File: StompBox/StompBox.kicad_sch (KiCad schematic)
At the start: 43 parts, among them J1 AudioJack2_Dual_Ground_Switch, J2 Barrel_Jack_Switch, J3 Conn_01x03, J4 AudioJack2_Dual_Ground_Switch, J5 BATT, SW1 ThreeWayStompBox, SW2 ThreeWayStompBox, SW3 ThreeWayStompBox, SW4 ThreeWayStompBox

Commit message: Stompbox JLCPCB
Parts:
- added H10, H11, H12, H9: MountingHole, MountingHole:MountingHole_3.2mm_M3, symbol Mechanical:MountingHole
- added J6: AudioJack2_Dual_Ground_Switch, StompBox:PJ-3240-35mm-stereo, symbol Connector:AudioJack2_Dual_Ground_Switch
- added R14: 10k, Resistor_THT:R_Axial_DIN0207_L6.3mm_D2.5mm_P7.62mm_Horizontal, symbol Device:R
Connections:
- net OUTVOLT is gone; now on net INVOLT: C1.1, J1.T1, J3.2 (Pin_2), JP2.1 (A)
- net GND: now also J6.G
- net at C3.1, J4.T1, R8.2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: now also R7.1, R14.1
- net at JP1.2 (B), R8.1: no longer R7.1
- new net: J6.T1, R14.2
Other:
- moved on the sheet: H1, H2, H3, H4, H5, H6, H7, H8

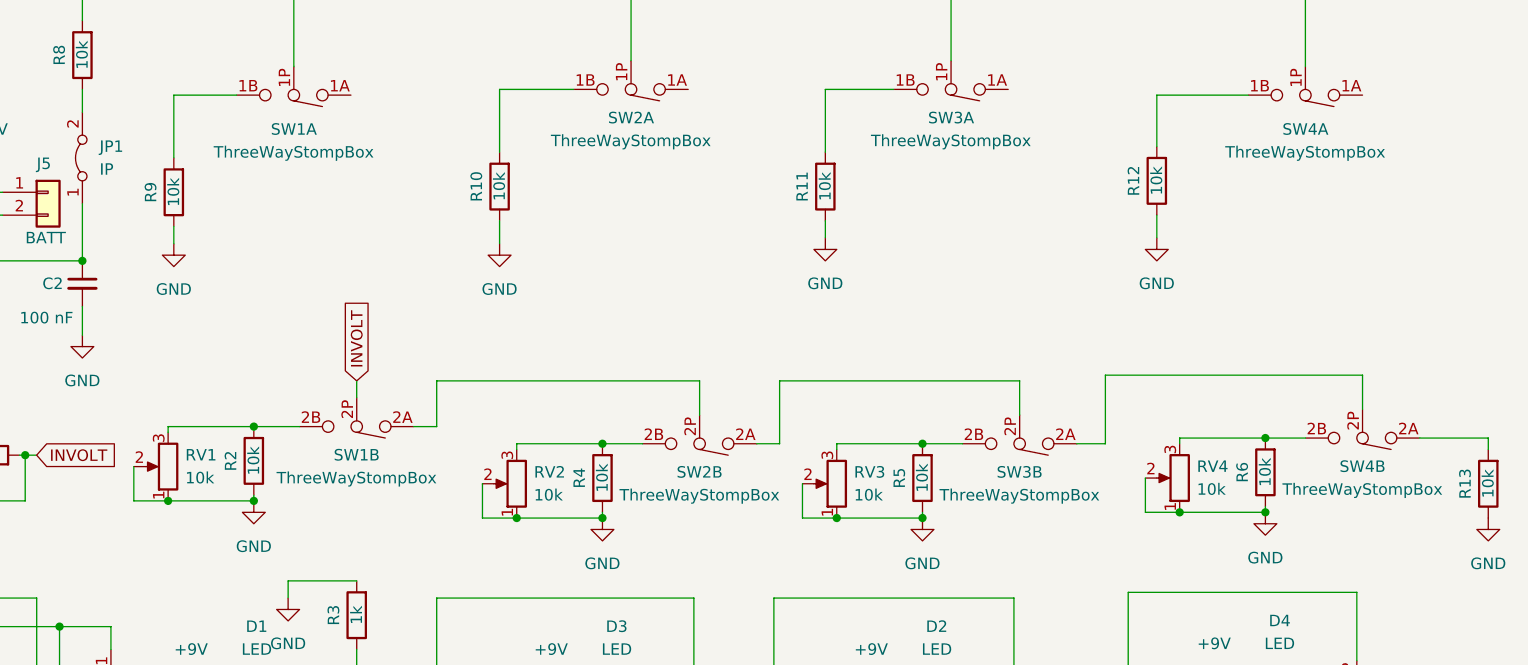
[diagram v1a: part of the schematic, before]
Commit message: Added support for stomp box
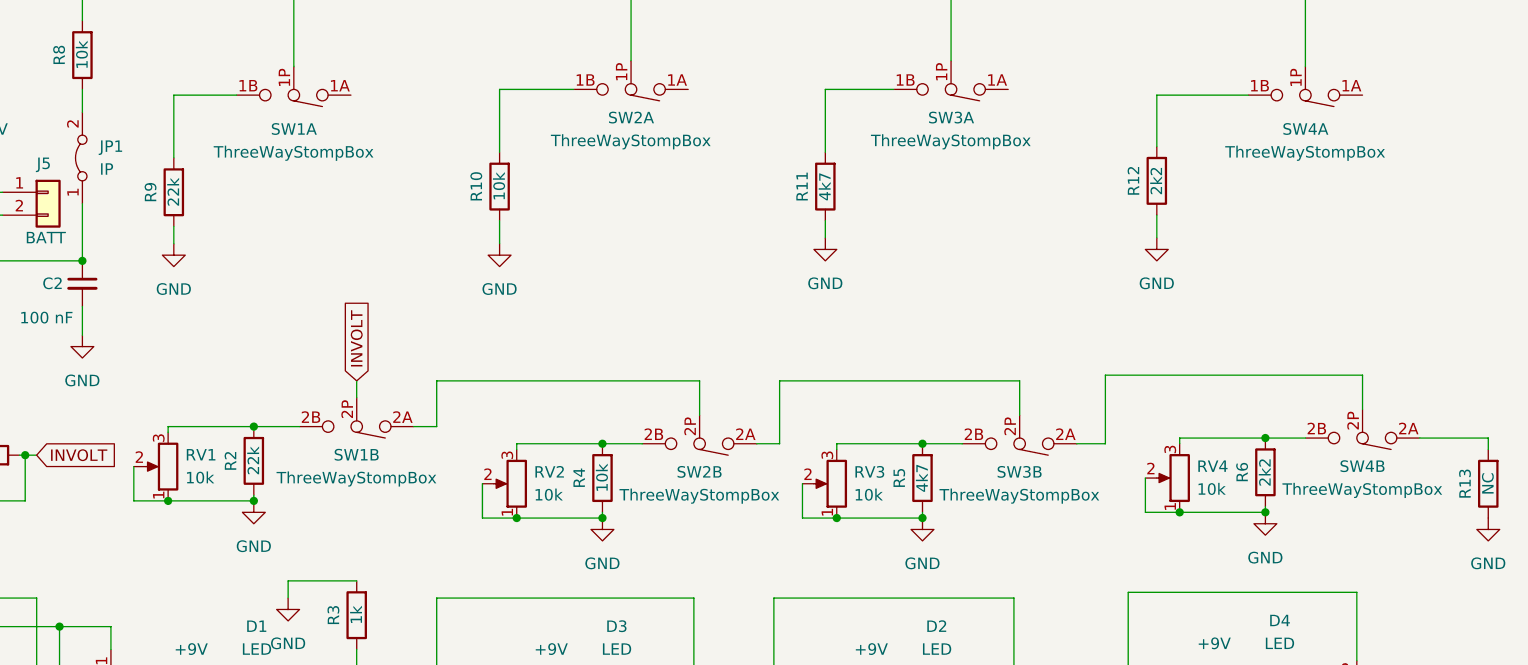
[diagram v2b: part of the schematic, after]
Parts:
- R11, R5: value 10k -> 4k7
- R12, R6: value 10k -> 2k2
- R13: value 10k -> NC
- R2, R9: value 10k -> 22k
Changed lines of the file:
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@@
     (in_bom yes) (on_board yes)
     (property "Reference" "R2" (id 0) (at 73.025 118.745 90))
-    (property "Value" "10k" (id 1) (at 75.565 118.745 90))
+    (property "Value" "22k" (id 1) (at 75.565 118.745 90))
     (property "Footprint" "Resistor_THT:R_Axial_DIN0207_L6.3mm_D2.5mm_P7.62mm_Horizontal" (id 2) (at 77.343 118.745 90)
       (effects (font (size 1.27 1.27)) hide)
@@
     (in_bom yes) (on_board yes)
     (property "Reference" "R5" (id 0) (at 147.32 120.65 90))
-    (property "Value" "10k" (id 1) (at 149.86 120.65 90))
+    (property "Value" "4k7" (id 1) (at 149.86 120.65 90))
     (property "Footprint" "Resistor_THT:R_Axial_DIN0207_L6.3mm_D2.5mm_P7.62mm_Horizontal" (id 2) (at 151.638 120.65 90)
       (effects (font (size 1.27 1.27)) hide)
@@
     (in_bom yes) (on_board yes)
     (property "Reference" "R12" (id 0) (at 173.355 87.63 90))
-    (property "Value" "10k" (id 1) (at 175.895 87.63 90))
+    (property "Value" "2k2" (id 1) (at 175.895 87.63 90))
     (property "Footprint" "Resistor_THT:R_Axial_DIN0207_L6.3mm_D2.5mm_P7.62mm_Horizontal" (id 2) (at 177.673 87.63 90)
       (effects (font (size 1.27 1.27)) hide)
@@
     (in_bom yes) (on_board yes)
     (property "Reference" "R13" (id 0) (at 210.185 121.285 90))
-    (property "Value" "10k" (id 1) (at 212.725 121.285 90))
+    (property "Value" "NC" (id 1) (at 212.725 121.285 90))
     (property "Footprint" "Resistor_THT:R_Axial_DIN0207_L6.3mm_D2.5mm_P7.62mm_Horizontal" (id 2) (at 214.503 121.285 90)
       (effects (font (size 1.27 1.27)) hide)
@@
     (in_bom yes) (on_board yes)
     (property "Reference" "R9" (id 0) (at 64.135 88.9 90))
-    (property "Value" "10k" (id 1) (at 66.675 88.9 90))
+    (property "Value" "22k" (id 1) (at 66.675 88.9 90))
     (property "Footprint" "Resistor_THT:R_Axial_DIN0207_L6.3mm_D2.5mm_P7.62mm_Horizontal" (id 2) (at 68.453 88.9 90)
       (effects (font (size 1.27 1.27)) hide)
@@
     (in_bom yes) (on_board yes)
     (property "Reference" "R11" (id 0) (at 136.525 88.265 90))
-    (property "Value" "10k" (id 1) (at 139.065 88.265 90))
+    (property "Value" "4k7" (id 1) (at 139.065 88.265 90))
     (property "Footprint" "Resistor_THT:R_Axial_DIN0207_L6.3mm_D2.5mm_P7.62mm_Horizontal" (id 2) (at 140.843 88.265 90)
       (effects (font (size 1.27 1.27)) hide)
@@
     (in_bom yes) (on_board yes)
     (property "Reference" "R6" (id 0) (at 185.42 120.015 90))
-    (property "Value" "10k" (id 1) (at 187.96 120.015 90))
+    (property "Value" "2k2" (id 1) (at 187.96 120.015 90))
     (property "Footprint" "Resistor_THT:R_Axial_DIN0207_L6.3mm_D2.5mm_P7.62mm_Horizontal" (id 2) (at 189.738 120.015 90)
       (effects (font (size 1.27 1.27)) hide)
@@
     )
     (path "/136b787d-27be-49e0-99c4-67c7e5f972d7"
-      (reference "R2") (unit 1) (value "10k") (footprint "Resistor_THT:R_Axial_DIN0207_L6.3mm_D2.5mm_P7.62mm_Horizontal")
+      (reference "R2") (unit 1) (value "22k") (footprint "Resistor_THT:R_Axial_DIN0207_L6.3mm_D2.5mm_P7.62mm_Horizontal")
     )
     (path "/61f59321-3b88-460b-bac6-5502f4f19220"
@@
     )
     (path "/46d55a27-2466-4d47-8df6-e279c2739c3e"
-      (reference "R5") (unit 1) (value "10k") (footprint "Resistor_THT:R_Axial_DIN0207_L6.3mm_D2.5mm_P7.62mm_Horizontal")
+      (reference "R5") (unit 1) (value "4k7") (footprint "Resistor_THT:R_Axial_DIN0207_L6.3mm_D2.5mm_P7.62mm_Horizontal")
     )
     (path "/e86f5408-e3d1-401c-8e6d-76243eacadc2"
-      (reference "R6") (unit 1) (value "10k") (footprint "Resistor_THT:R_Axial_DIN0207_L6.3mm_D2.5mm_P7.62mm_Horizontal")
+      (reference "R6") (unit 1) (value "2k2") (footprint "Resistor_THT:R_Axial_DIN0207_L6.3mm_D2.5mm_P7.62mm_Horizontal")
     )
     (path "/a3e5b188-939f-47a3-b82e-21b82cd259e3"
@@
     )
     (path "/6e8309de-e9f7-463b-b88b-41bcd21a3f1d"
-      (reference "R9") (unit 1) (value "10k") (footprint "Resistor_THT:R_Axial_DIN0207_L6.3mm_D2.5mm_P7.62mm_Horizontal")
+      (reference "R9") (unit 1) (value "22k") (footprint "Resistor_THT:R_Axial_DIN0207_L6.3mm_D2.5mm_P7.62mm_Horizontal")
     )
     (path "/5279d011-4b30-4ce5-a7f0-eafbd78a727d"
@@
     )
     (path "/7e3a131b-14b8-44a2-81f3-f9499f1ba97f"
-      (reference "R11") (unit 1) (value "10k") (footprint "Resistor_THT:R_Axial_DIN0207_L6.3mm_D2.5mm_P7.62mm_Horizontal")
+      (reference "R11") (unit 1) (value "4k7") (footprint "Resistor_THT:R_Axial_DIN0207_L6.3mm_D2.5mm_P7.62mm_Horizontal")
     )
     (path "/51948780-b0b4-4954-844b-4e2753e251ac"
-      (reference "R12") (unit 1) (value "10k") (footprint "Resistor_THT:R_Axial_DIN0207_L6.3mm_D2.5mm_P7.62mm_Horizontal")
+      (reference "R12") (unit 1) (value "2k2") (footprint "Resistor_THT:R_Axial_DIN0207_L6.3mm_D2.5mm_P7.62mm_Horizontal")
     )
     (path "/586872a7-96d4-42b1-b63d-b31c1f755a42"
-      (reference "R13") (unit 1) (value "10k") (footprint "Resistor_THT:R_Axial_DIN0207_L6.3mm_D2.5mm_P7.62mm_Horizontal")
+      (reference "R13") (unit 1) (value "NC") (footprint "Resistor_THT:R_Axial_DIN0207_L6.3mm_D2.5mm_P7.62mm_Horizontal")
     )
     (path "/afd6490c-df31-4805-b50a-a1379dae9086"
